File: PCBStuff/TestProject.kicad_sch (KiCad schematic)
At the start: 6 parts

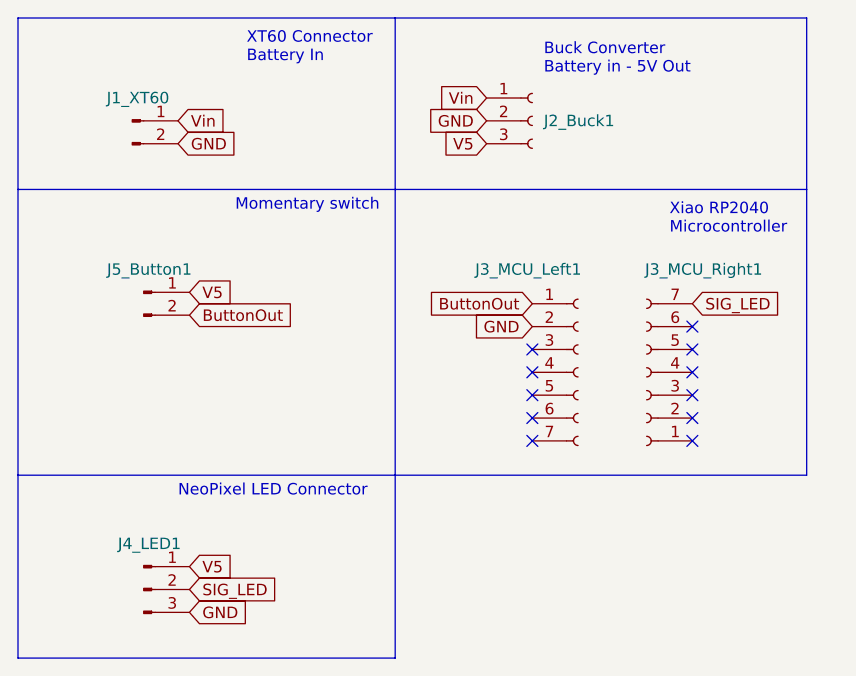
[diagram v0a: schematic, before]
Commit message: Made new gerbers including drillfile to make holes in jlcpcb
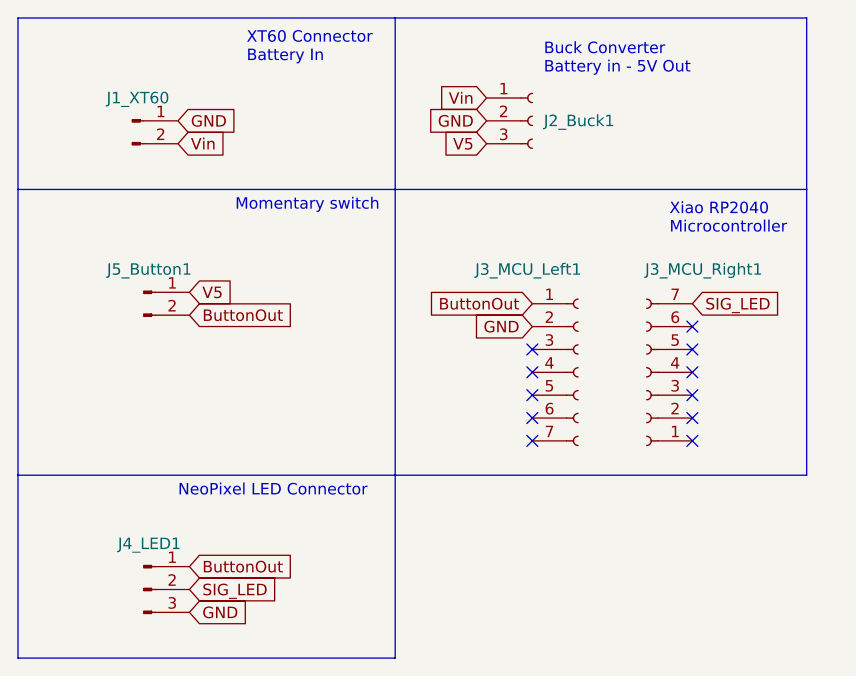
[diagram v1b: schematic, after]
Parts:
- J1_XT60: value (none) -> Conn_01x02_Male; footprint (none) -> Connector_AMASS:AMASS_XT60-M_1x02_P7.20mm_Vertical
- J2_Buck1: value (none) -> Conn_01x03_Female; footprint (none) -> Connector_PinSocket_2.54mm:PinSocket_1x03_P2.54mm_Vertical
- J3_MCU_Left1, J3_MCU_Right1: value (none) -> Conn_01x07_Female; footprint (none) -> Connector_PinSocket_2.54mm:PinSocket_1x07_P2.54mm_Vertical
- J4_LED1: value (none) -> Conn_01x03_Male; footprint (none) -> Connector_PinSocket_2.54mm:PinSocket_1x03_P2.54mm_Vertical
- J5_Button1: value (none) -> Conn_01x02_Male; footprint (none) -> Connector_PinHeader_2.54mm:PinHeader_1x02_P2.54mm_Vertical
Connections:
- net ButtonOut: now also J4_LED1.1 (Pin_1)
- net GND: now also J1_XT60.1 (Pin_1); no longer J1_XT60.2 (Pin_2)
- net V5: no longer J4_LED1.1 (Pin_1)
- net Vin: now also J1_XT60.2 (Pin_2); no longer J1_XT60.1 (Pin_1)
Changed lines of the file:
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@@
     )
   )
-  (global_label "Vin" (shape input) (at 30.48 24.13 0) (fields_autoplaced)
+  (global_label "GND" (shape input) (at 30.48 24.13 0) (fields_autoplaced)
     (effects (font (size 1.27 1.27)) (justify left))
-    (property "Intersheet References" "${INTERSHEET_REFS}" (id 0) (at 35.7355 24.0506 0)
+    (property "Intersheet References" "${INTERSHEET_REFS}" (id 0) (at 36.7636 24.0506 0)
       (effects (font (size 1.27 1.27)) (justify left) hide)
     )
   )
-  (global_label "GND" (shape input) (at 30.48 26.67 0) (fields_autoplaced)
+  (global_label "Vin" (shape input) (at 30.48 26.67 0) (fields_autoplaced)
     (effects (font (size 1.27 1.27)) (justify left))
-    (property "Intersheet References" "${INTERSHEET_REFS}" (id 0) (at 36.7636 26.5906 0)
+    (property "Intersheet References" "${INTERSHEET_REFS}" (id 0) (at 35.7355 26.5906 0)
       (effects (font (size 1.27 1.27)) (justify left) hide)
     )
@@
     )
   )
-  (global_label "V5" (shape input) (at 31.75 73.66 0) (fields_autoplaced)
+  (global_label "ButtonOut" (shape input) (at 31.75 73.66 0) (fields_autoplaced)
     (effects (font (size 1.27 1.27)) (justify left))
-    (property "Intersheet References" "${INTERSHEET_REFS}" (id 0) (at 36.4612 73.5806 0)
+    (property "Intersheet References" "${INTERSHEET_REFS}" (id 0) (at 43.5369 73.5806 0)
       (effects (font (size 1.27 1.27)) (justify left) hide)
     )
@@
     (in_bom yes) (on_board yes) (fields_autoplaced)
     (property "Reference" "J5_Button1" (id 0) (at 27.305 40.64 0))
-    (property "Value" "" (id 1) (at 27.305 40.64 0)
+    (property "Value" "Conn_01x02_Male" (id 1) (at 27.305 40.64 0)
       (effects (font (size 1.27 1.27)) hide)
     )
-    (property "Footprint" "" (id 2) (at 26.67 43.18 0)
+    (property "Footprint" "Connector_PinHeader_2.54mm:PinHeader_1x02_P2.54mm_Vertical" (id 2) (at 26.67 43.18 0)
       (effects (font (size 1.27 1.27)) hide)
     )
@@
       (effects (font (size 1.27 1.27)) (justify left))
     )
-    (property "Value" "" (id 1) (at 69.215 29.21 0)
+    (property "Value" "Conn_01x03_Female" (id 1) (at 69.215 29.21 0)
       (effects (font (size 1.27 1.27)) hide)
     )
-    (property "Footprint" "" (id 2) (at 69.85 24.13 0)
+    (property "Footprint" "Connector_PinSocket_2.54mm:PinSocket_1x03_P2.54mm_Vertical" (id 2) (at 69.85 24.13 0)
       (effects (font (size 1.27 1.27)) hide)
     )
@@
       (effects (font (size 1.27 1.27)) (justify left))
     )
-    (property "Value" "" (id 1) (at 64.77 41.91 0)
+    (property "Value" "Conn_01x07_Female" (id 1) (at 64.77 41.91 0)
       (effects (font (size 1.27 1.27)) (justify left) hide)
     )
-    (property "Footprint" "" (id 2) (at 74.93 52.07 0)
+    (property "Footprint" "Connector_PinSocket_2.54mm:PinSocket_1x07_P2.54mm_Vertical" (id 2) (at 74.93 52.07 0)
       (effects (font (size 1.27 1.27)) hide)
     )
@@
     (in_bom yes) (on_board yes)
     (property "Reference" "J3_MCU_Right1" (id 0) (at 88.9 40.64 0))
-    (property "Value" "" (id 1) (at 83.185 41.91 0)
+    (property "Value" "Conn_01x07_Female" (id 1) (at 83.185 41.91 0)
       (effects (font (size 1.27 1.27)) hide)
     )
-    (property "Footprint" "" (id 2) (at 82.55 52.07 0)
+    (property "Footprint" "Connector_PinSocket_2.54mm:PinSocket_1x07_P2.54mm_Vertical" (id 2) (at 82.55 52.07 0)
       (effects (font (size 1.27 1.27)) hide)
     )
@@
     (in_bom yes) (on_board yes) (fields_autoplaced)
     (property "Reference" "J4_LED1" (id 0) (at 27.305 71.12 0))
-    (property "Value" "" (id 1) (at 27.305 71.12 0)
+    (property "Value" "Conn_01x03_Male" (id 1) (at 27.305 71.12 0)
       (effects (font (size 1.27 1.27)) hide)
     )
-    (property "Footprint" "" (id 2) (at 26.67 76.2 0)
+    (property "Footprint" "Connector_PinSocket_2.54mm:PinSocket_1x03_P2.54mm_Vertical" (id 2) (at 26.67 76.2 0)
       (effects (font (size 1.27 1.27)) hide)
     )
@@
     (in_bom yes) (on_board yes) (fields_autoplaced)
     (property "Reference" "J1_XT60" (id 0) (at 26.035 21.59 0))
-    (property "Value" "" (id 1) (at 26.035 21.59 0)
+    (property "Value" "Conn_01x02_Male" (id 1) (at 26.035 21.59 0)
       (effects (font (size 1.27 1.27)) hide)
     )
-    (property "Footprint" "" (id 2) (at 25.4 24.13 0)
+    (property "Footprint" "Connector_AMASS:AMASS_XT60-M_1x02_P7.20mm_Vertical" (id 2) (at 25.4 24.13 0)
       (effects (font (size 1.27 1.27)) hide)
     )

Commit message: Fixed footprint of MCU, re-organized header layout to shrink overall boardsize
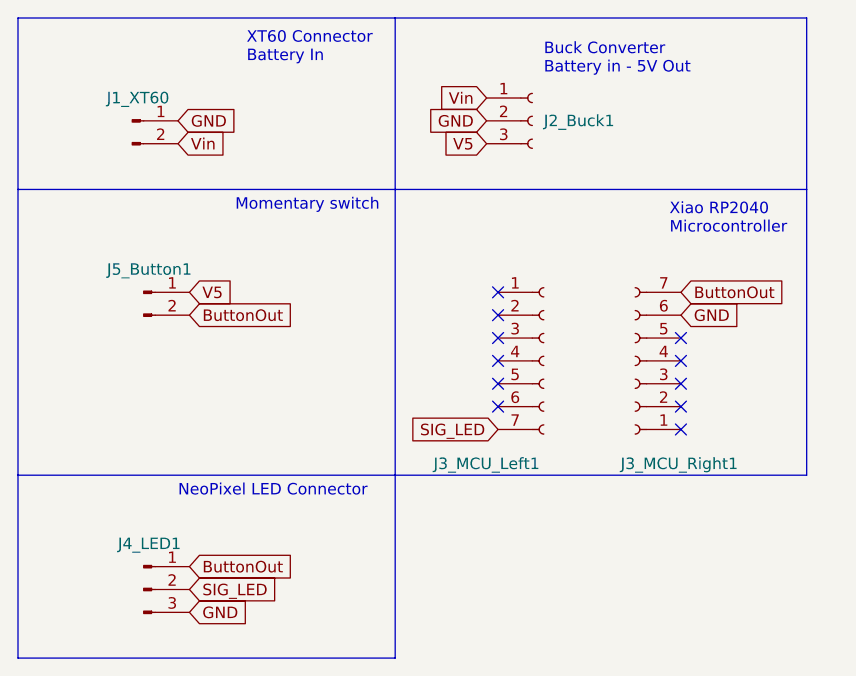
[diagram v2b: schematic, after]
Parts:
- J4_LED1: footprint Connector_PinSocket_2.54mm:PinSocket_1x03_P2.54mm_Vertical -> (none)
- renumbered J3_MCU_Right1 to J3_MCU_Left1, J3_MCU_Left1 to J3_MCU_Right1
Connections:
- net ButtonOut: now also J3_MCU_Right1.7 (Pin_7); no longer J3_MCU_Right1.1 (Pin_1)
- net GND: now also J3_MCU_Right1.6 (Pin_6); no longer J3_MCU_Right1.2 (Pin_2)
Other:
- moved on the sheet: J3_MCU_Left1, J3_MCU_Right1
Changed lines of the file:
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@@
 (kicad_sch (version 20211123) (generator eeschema)
   (paper "A4")
-  (no_connect (at 87.63 59.69))
-  (no_connect (at 69.85 59.69))
-  (no_connect (at 87.63 57.15))
-  (no_connect (at 87.63 46.99))
-  (no_connect (at 87.63 52.07))
-  (no_connect (at 87.63 54.61))
-  (no_connect (at 87.63 49.53))
-  (no_connect (at 69.85 57.15))
-  (no_connect (at 69.85 49.53))
-  (no_connect (at 69.85 54.61))
-  (no_connect (at 69.85 52.07))
+  (no_connect (at 66.04 43.18))
+  (no_connect (at 86.36 55.88))
+  (no_connect (at 66.04 45.72))
+  (no_connect (at 66.04 55.88))
+  (no_connect (at 66.04 50.8))
+  (no_connect (at 66.04 48.26))
+  (no_connect (at 66.04 53.34))
+  (no_connect (at 86.36 58.42))
+  (no_connect (at 86.36 53.34))
+  (no_connect (at 86.36 48.26))
+  (no_connect (at 86.36 50.8))
   (polyline (pts (xy 54.61 63.5) (xy 100.33 63.5))
     (stroke (width 0) (type default) (color 0 0 0 0))
@@
     )
   )
-  (global_label "GND" (shape input) (at 69.85 46.99 180) (fields_autoplaced)
-    (effects (font (size 1.27 1.27)) (justify right))
-    (property "Intersheet References" "${INTERSHEET_REFS}" (id 0) (at 63.5664 46.9106 0)
-      (effects (font (size 1.27 1.27)) (justify right) hide)
+  (global_label "GND" (shape input) (at 86.36 45.72 0) (fields_autoplaced)
+    (effects (font (size 1.27 1.27)) (justify left))
+    (property "Intersheet References" "${INTERSHEET_REFS}" (id 0) (at 92.6436 45.7994 0)
+      (effects (font (size 1.27 1.27)) (justify left) hide)
     )
   )
@@
     )
   )
-  (global_label "SIG_LED" (shape input) (at 87.63 44.45 0) (fields_autoplaced)
-    (effects (font (size 1.27 1.27)) (justify left))
-    (property "Intersheet References" "${INTERSHEET_REFS}" (id 0) (at 97.5421 44.3706 0)
-      (effects (font (size 1.27 1.27)) (justify left) hide)
+  (global_label "SIG_LED" (shape input) (at 66.04 58.42 180) (fields_autoplaced)
+    (effects (font (size 1.27 1.27)) (justify right))
+    (property "Intersheet References" "${INTERSHEET_REFS}" (id 0) (at 56.1279 58.4994 0)
+      (effects (font (size 1.27 1.27)) (justify right) hide)
     )
   )
@@
     )
   )
-  (global_label "ButtonOut" (shape input) (at 69.85 44.45 180) (fields_autoplaced)
-    (effects (font (size 1.27 1.27)) (justify right))
-    (property "Intersheet References" "${INTERSHEET_REFS}" (id 0) (at 58.0631 44.3706 0)
-      (effects (font (size 1.27 1.27)) (justify right) hide)
+  (global_label "ButtonOut" (shape input) (at 86.36 43.18 0) (fields_autoplaced)
+    (effects (font (size 1.27 1.27)) (justify left))
+    (property "Intersheet References" "${INTERSHEET_REFS}" (id 0) (at 98.1469 43.2594 0)
+      (effects (font (size 1.27 1.27)) (justify left) hide)
     )
   )
@@
     (pin "3")
   )
-  (symbol (lib_id "Connector:Conn_01x07_Female") (at 74.93 52.07 0) (unit 1)
+  (symbol (lib_id "Connector:Conn_01x07_Female") (at 81.28 50.8 180) (unit 1)
     (in_bom yes) (on_board yes)
-    (property "Reference" "J3_MCU_Left1" (id 0) (at 63.5 40.64 0)
+    (property "Reference" "J3_MCU_Right1" (id 0) (at 92.71 62.23 0)
       (effects (font (size 1.27 1.27)) (justify left))
     )
-    (property "Value" "Conn_01x07_Female" (id 1) (at 64.77 41.91 0)
-      (effects (font (size 1.27 1.27)) (justify left) hide)
-    )
-    (property "Footprint" "Connector_PinSocket_2.54mm:PinSocket_1x07_P2.54mm_Vertical" (id 2) (at 74.93 52.07 0)
-      (effects (font (size 1.27 1.27)) hide)
-    )
-    (property "Datasheet" "~" (id 3) (at 74.93 52.07 0)
+    (property "Value" "Conn_01x07_Female" (id 1) (at 91.44 60.96 0)
+      (effects (font (size 1.27 1.27)) (justify left) hide)
+    )
+    (property "Footprint" "Connector_PinSocket_2.54mm:PinSocket_1x07_P2.54mm_Vertical" (id 2) (at 81.28 50.8 0)
+      (effects (font (size 1.27 1.27)) hide)
+    )
+    (property "Datasheet" "~" (id 3) (at 81.28 50.8 0)
       (effects (font (size 1.27 1.27)) hide)
     )
@@
     (pin "7")
   )
-  (symbol (lib_id "Connector:Conn_01x07_Female") (at 82.55 52.07 180) (unit 1)
+  (symbol (lib_id "Connector:Conn_01x07_Female") (at 71.12 50.8 0) (unit 1)
     (in_bom yes) (on_board yes)
-    (property "Reference" "J3_MCU_Right1" (id 0) (at 88.9 40.64 0))
-    (property "Value" "Conn_01x07_Female" (id 1) (at 83.185 41.91 0)
-      (effects (font (size 1.27 1.27)) hide)
-    )
-    (property "Footprint" "Connector_PinSocket_2.54mm:PinSocket_1x07_P2.54mm_Vertical" (id 2) (at 82.55 52.07 0)
-      (effects (font (size 1.27 1.27)) hide)
-    )
-    (property "Datasheet" "~" (id 3) (at 82.55 52.07 0)
+    (property "Reference" "J3_MCU_Left1" (id 0) (at 64.77 62.23 0))
+    (property "Value" "Conn_01x07_Female" (id 1) (at 70.485 60.96 0)
+      (effects (font (size 1.27 1.27)) hide)
+    )
+    (property "Footprint" "Connector_PinSocket_2.54mm:PinSocket_1x07_P2.54mm_Vertical" (id 2) (at 71.12 50.8 0)
+      (effects (font (size 1.27 1.27)) hide)
+    )
+    (property "Datasheet" "~" (id 3) (at 71.12 50.8 0)
       (effects (font (size 1.27 1.27)) hide)
     )
@@
       (effects (font (size 1.27 1.27)) hide)
     )
-    (property "Footprint" "Connector_PinSocket_2.54mm:PinSocket_1x03_P2.54mm_Vertical" (id 2) (at 26.67 76.2 0)
+    (property "Footprint" "" (id 2) (at 26.67 76.2 0)
       (effects (font (size 1.27 1.27)) hide)
     )
@@
       (reference "J2_Buck1") (unit 1) (value "Conn_01x03_Female") (footprint "Connector_PinSocket_2.54mm:PinSocket_1x03_P2.54mm_Vertical")
     )
+    (path "/8cb0adaa-acd2-4046-aef3-2e8849a59b9f"
+      (reference "J3_MCU_Left1") (unit 1) (value "Conn_01x07_Female") (footprint "Connector_PinSocket_2.54mm:PinSocket_1x07_P2.54mm_Vertical")
+    )
     (path "/7981c0ba-a5a0-4ab9-a2ee-681c264b45da"
-      (reference "J3_MCU_Left1") (unit 1) (value "Conn_01x07_Female") (footprint "Connector_PinSocket_2.54mm:PinSocket_1x07_P2.54mm_Vertical")
-    )
-    (path "/8cb0adaa-acd2-4046-aef3-2e8849a59b9f"
       (reference "J3_MCU_Right1") (unit 1) (value "Conn_01x07_Female") (footprint "Connector_PinSocket_2.54mm:PinSocket_1x07_P2.54mm_Vertical")
     )
     (path "/c11ca3bc-a8bb-430a-9e10-289b52cce878"
-      (reference "J4_LED1") (unit 1) (value "Conn_01x03_Male") (footprint "Connector_PinSocket_2.54mm:PinSocket_1x03_P2.54mm_Vertical")
+      (reference "J4_LED1") (unit 1) (value "Conn_01x03_Male") (footprint "Connector_PinHeader_2.54mm:PinHeader_1x03_P2.54mm_Vertical")
     )
     (path "/222a1c0d-2693-4802-ada8-5b0adcf96f0c"
